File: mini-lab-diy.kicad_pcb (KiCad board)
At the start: 2 copper layers, 98.3 x 98.7 mm, 71 parts, among them J1 Conn_01x20, J2 Conn_01x20, M1 Motor_Servo, SW1 SW_Push_Dual, SW2 SW_Push_Dual, SW3 SW_Push_Dual, SW4 SW_Push_Dual, U3 FRANZININHO_WIFI_PINOUT

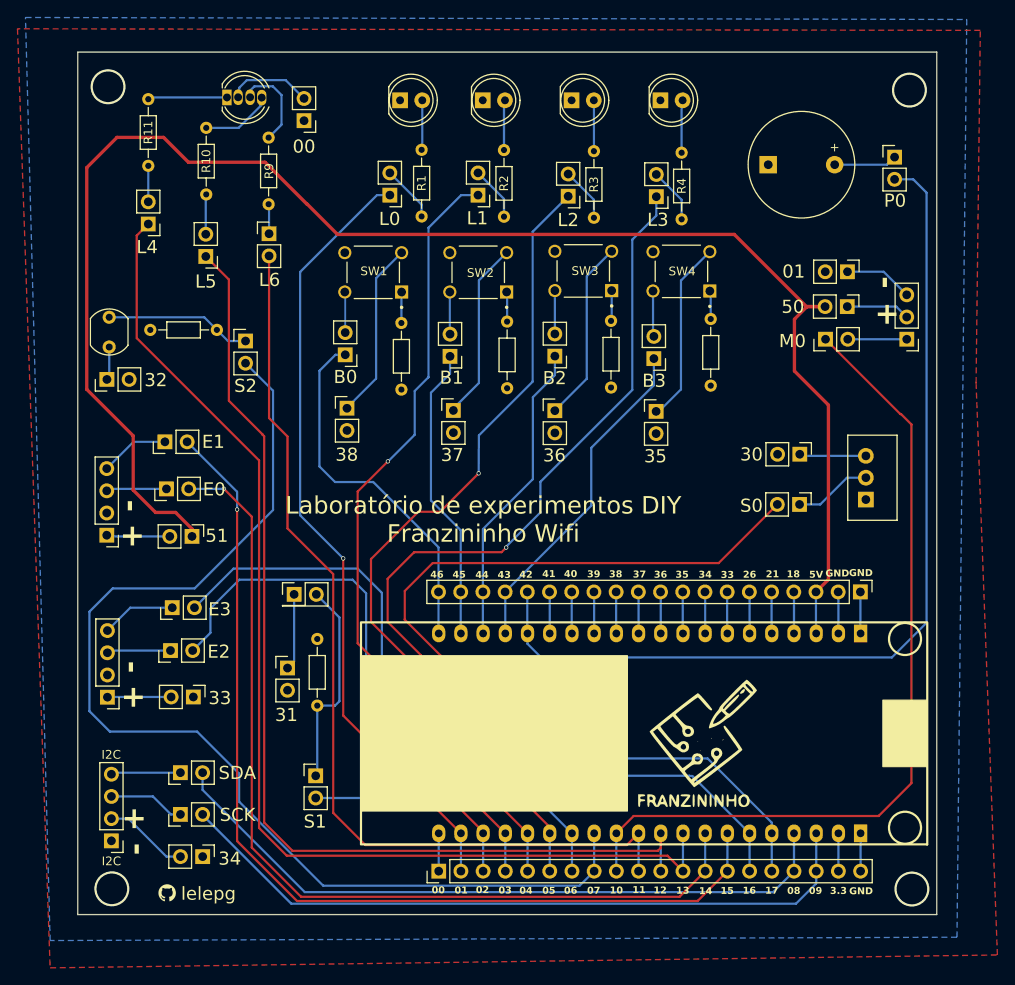
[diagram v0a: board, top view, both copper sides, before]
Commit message: modificação de orientação de alguns pads
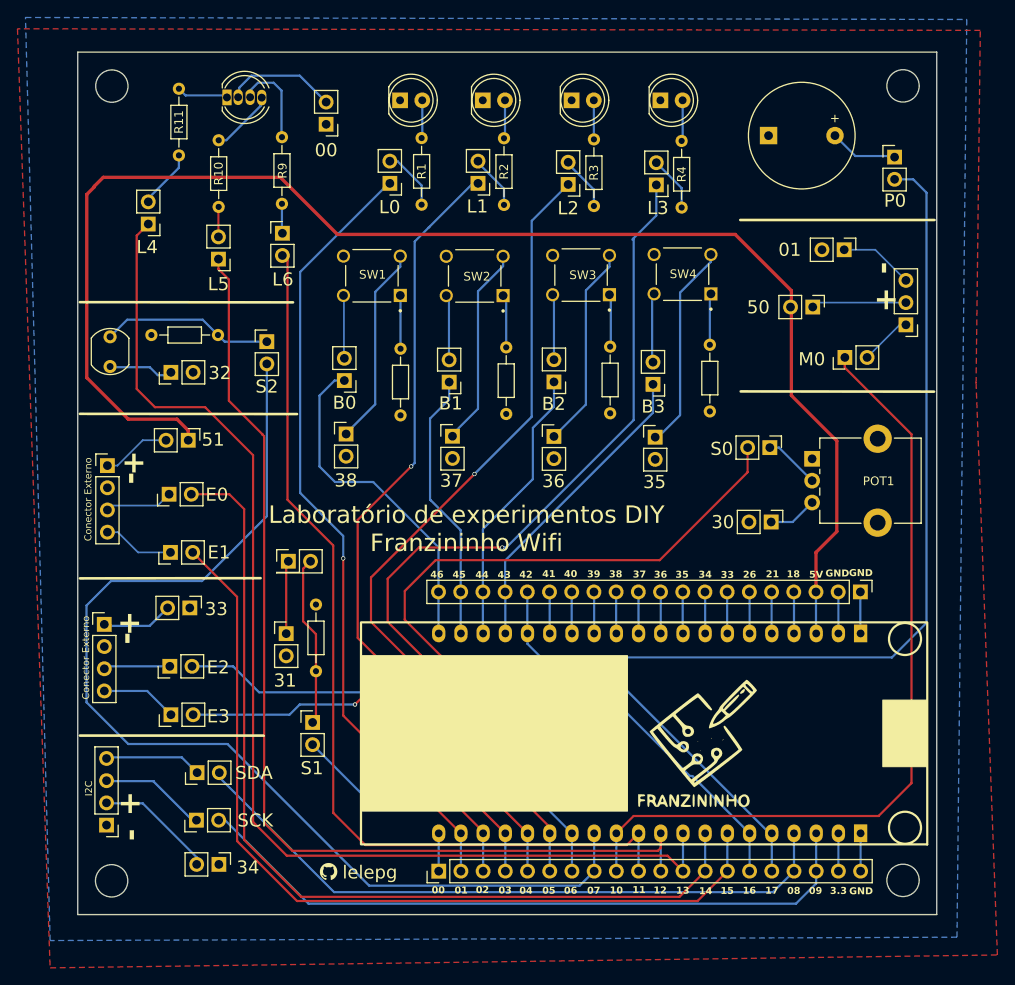
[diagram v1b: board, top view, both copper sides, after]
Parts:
- added REF**: MountingHole_3.7mm, MountingHole:MountingHole_3.7mm, F.Cu at (29.6, 24.2)
- added REF**: MountingHole_3.7mm, MountingHole:MountingHole_3.7mm, F.Cu at (29.6, 115.1)
- added REF**: MountingHole_3.7mm, MountingHole:MountingHole_3.7mm, F.Cu at (120.1, 24.2)
- added REF**: MountingHole_3.7mm, MountingHole:MountingHole_3.7mm, F.Cu at (120.1, 115.1)
- POT1: footprint Potentiometer_THT:Potentiometer_Alps_RK09Y11_Single_Horizontal -> Potentiometer_THT:Potentiometer_Alpha_RD901F-40-00D_Single_Vertical_CircularHoles
- moved G*** 18.6 mm to (54.4, 114.1)
- moved G*** 18.6 mm to (61.4, 114.1)
- moved EnableE1 12.7 mm to (36.3, 77.6)
- moved EnableE3 12.2 mm to (36.4, 96.1)
- moved Enable51 11.0 mm to (38.4, 64.7)
- moved Enable33 10.2 mm to (38.6, 83.9)
- moved Enable30 8.41 mm to (105.1, 74.1)
- moved Jumpers2 8.34 mm to (28.8, 85.8), turned to 0 degrees
- moved Jumpers1 7.97 mm to (29.1, 67.6), turned to 0 degrees
- moved POT1 7.71 mm to (109.7, 66.9), turned to 0 degrees
- moved Enable32 7.37 mm to (36.4, 57.0)
- moved EnableS0 7.34 mm to (104.9, 65.6)
- moved EnableS1 6.11 mm to (52.6, 97.0)
- moved Enable50 3.95 mm to (109.8, 49.5)
- moved Enable31 3.94 mm to (49.6, 86.9)
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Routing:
- net +5V: track 184.6 -> 165.3 mm
- net 16: track 90.2 -> 76.0 mm
- net 15: track 112.7 -> 99.8 mm, vias 1 -> 0
- net 17: track 90.1 -> 79.6 mm, vias 0 -> 2
- net Net-(EnableS1-Pin_1): track 23.9 -> 19.6 mm
- net Net-(Enable34-Pin_2): track 9.70 -> 13.9 mm
- net Net-(EnableSCK0-Pin_1): track 8.75 -> 12.9 mm
- net Net-(EnableSDA0-Pin_1): track 7.72 -> 11.6 mm
- net Net-(Enable32-Pin_1): track 3.45 -> 7.04 mm
- net Net-(Enable50-Pin_1): track 7.30 -> 10.9 mm
- net 13: track 130.3 -> 133.7 mm
- net Net-(LED5-RK): track 8.92 -> 5.66 mm
- net Net-(Enable0-Pin_2): track 9.73 -> 12.9 mm
- net Net-(EnableS2-Pin_1): track 16.7 -> 19.8 mm
- net 44: track 35.1 -> 32.1 mm
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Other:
- board text added: "Conector Externo"

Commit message: retirada dos gnd do led rgb e do motor, e aumento no espaçamento dos dados da silk
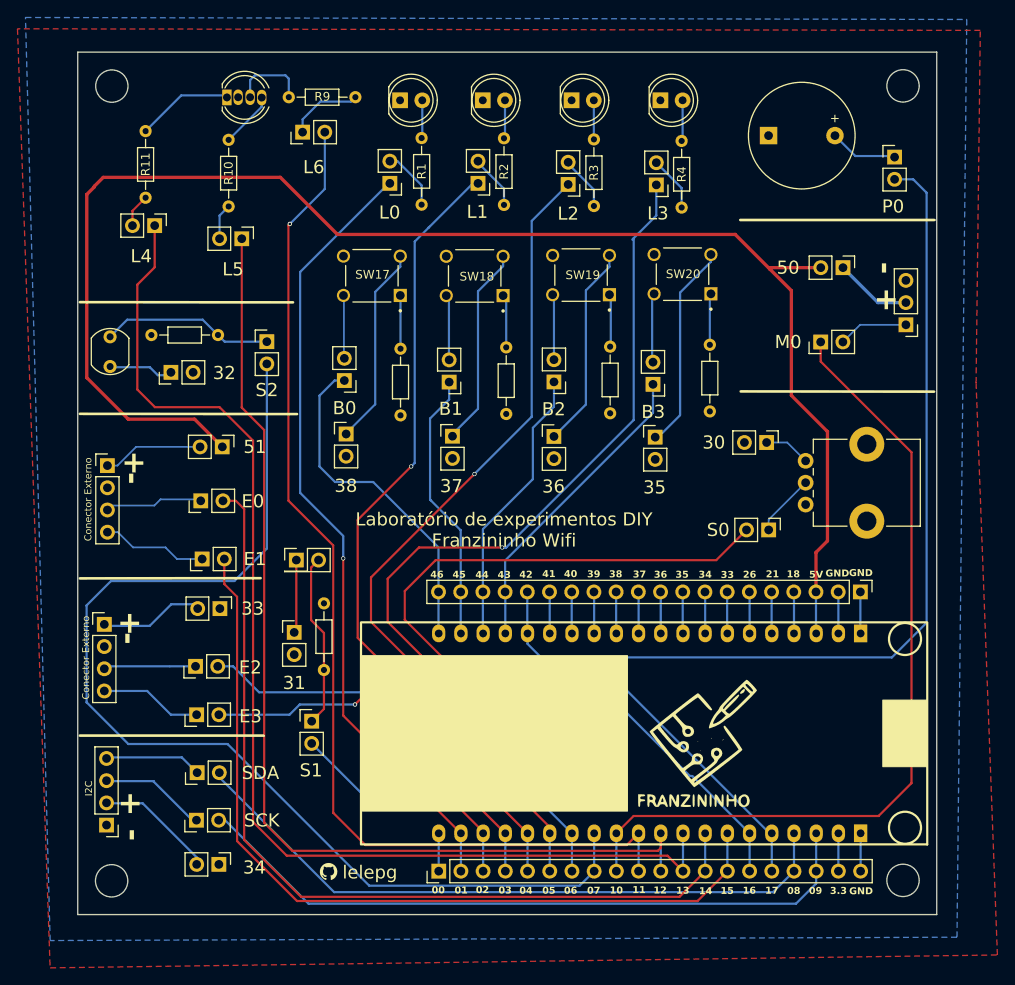
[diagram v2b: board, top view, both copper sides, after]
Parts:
- removed Enable0, Enable1: Conn_01x02, Connector_PinHeader_2.54mm:PinHeader_1x02_P2.54mm_Vertical
- POT1: footprint Potentiometer_THT:Potentiometer_Alpha_RD901F-40-00D_Single_Vertical_CircularHoles -> Potentiometer_THT:Potentiometer_Bourns_PTV09A-1_Single_Vertical
- moved R9 14.8 mm to (57.5, 25.5), turned to 180 degrees
- moved EnableL6 11.8 mm to (51.5, 29.5), turned to 90 degrees
- moved EnableS0 9.42 mm to (104.8, 75.0)
- moved Enable30 9.11 mm to (104.5, 65.0)
- moved R11 6.16 mm to (33.5, 37.0)
- moved Enable50 5.68 mm to (113.3, 45.0)
- moved POT1 5.29 mm to (109.0, 72.1)
- moved Enable51 3.97 mm to (42.3, 65.5)
- moved EnableE0 3.70 mm to (39.8, 71.7)
- moved EnableE1 3.70 mm to (40.0, 78.3)
- moved EnableL5 3.54 mm to (44.5, 41.7), turned to -90 degrees
- moved Enable33 3.44 mm to (42.0, 84.0)
- moved EnableM0 3.29 mm to (110.7, 53.5)
- moved EnableE2 2.94 mm to (39.2, 90.6)
- moved EnableE3 2.94 mm to (39.3, 96.1)
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- renumbered SW1 to SW17, SW2 to SW18, SW3 to SW19, SW4 to SW20, I2C to Tela1
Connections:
- LED5 pad 4: Net-(Enable0-Pin_2) -> GND
- M1 pad 3: Net-(Enable1-Pin_1) -> GND
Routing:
- net 11: track 107.5 -> 123.0 mm, vias 0 -> 1
- net Net-(Enable0-Pin_2): track 12.9 -> 0.00 mm
- net Net-(Enable1-Pin_1): track 8.69 -> 0.00 mm
- net +5V: track 165.3 -> 173.9 mm
- net 05: track 85.9 -> 80.2 mm
- net Net-(LED5-RK): track 5.66 -> 11.2 mm
- net Net-(EnableL6-Pin_1): track 3.39 -> 8.55 mm
- net 14: track 105.6 -> 101.6 mm
- net Net-(EnableE1-Pin_1): track 8.17 -> 12.1 mm
- net Net-(Enable33-Pin_2): track 8.16 -> 12.0 mm
- net Net-(Enable51-Pin_2): track 7.90 -> 11.5 mm
- net Net-(EnableE0-Pin_1): track 7.80 -> 11.3 mm
- net Net-(EnableL4-Pin_2): track 6.77 -> 3.81 mm
- net 17: track 79.6 -> 76.7 mm
- net Net-(EnableE3-Pin_1): track 8.75 -> 11.7 mm
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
